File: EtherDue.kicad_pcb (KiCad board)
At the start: 4 copper layers, 185 x 104 mm, 619 parts, among them IC201 ATSAM3X8E, IC301 ATMEGA16U2, IC601 W5100, P101 CONN_02X04, P102 MSTBV3, P103 MSTBV3, P104 MSTBV6, P1101 CONN_01X02, P1102 CONN_01X02, P1201 CONN_01X02, P1202 CONN_01X02, P1301 CONN_01X02, P1302 CONN_01X02, P1401 CONN_01X02, P1402 CONN_01X02, P301 USB_5PIN_SHELL, P401 USB_5PIN_SHELL, P801 MSTBV2, P901 677006144621, P902 677006144621, Q1001 BSS308, Q101 IPB020NE7N3G, Q102 IPB020NE7N3G, Q1501 BSS123, Q1502 BSS123, Q1601 BSS123, Q1602 BSS123, Q1701 BSS123, Q1702 BSS123, Q1703 BSS308, Q1704 BSS308, Q1801 BSS123, Q1802 BSS123, Q1803 BSS308, Q1804 BSS308, Q1901 BSS123, Q1902 BSS123, Q1903 BSS308, Q1904 BSS308, Q501 BC847BSMD, Q601 2N7002, SW1701 SW_PUSH, SW1801 SW_PUSH, SW1901 SW_PUSH, SW201 ERASE, SW202 RESET, U1001 AD7294BSUZ, U101 AD7415, U1101 ADL5513, U1102 REG101NA-5, U1201 ADL5513, U1202 REG101NA-5, U1301 ADL5513, U1302 REG101NA-5, U1401 ADL5513, U1402 REG101NA-5, U1501 4013_with_supply, U1701 MCP6H04, U1702 INA207, U1703 MEU1S1212ZC, U1801 INA207, U1802 MEU1S1212ZC, U1901 INA207, U1902 MEU1S1212ZC, U202 FDN340P, U203 LMV358IPWR, U501 POWERJACK, U502 LM2734Y, U503 FDN340P, U504 FDN340P, U505 NCP1117ST33T3G, U602 HY931147C, U603 APX811-31UG-7, U701 MICROSD, U702 24AA025E48, U801 TPS7A4501DCQT, U802 TPS7A4501DCQT, U803 TPS7A4501DCQT, U804 REG101NA-5, U901 TJA1040T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

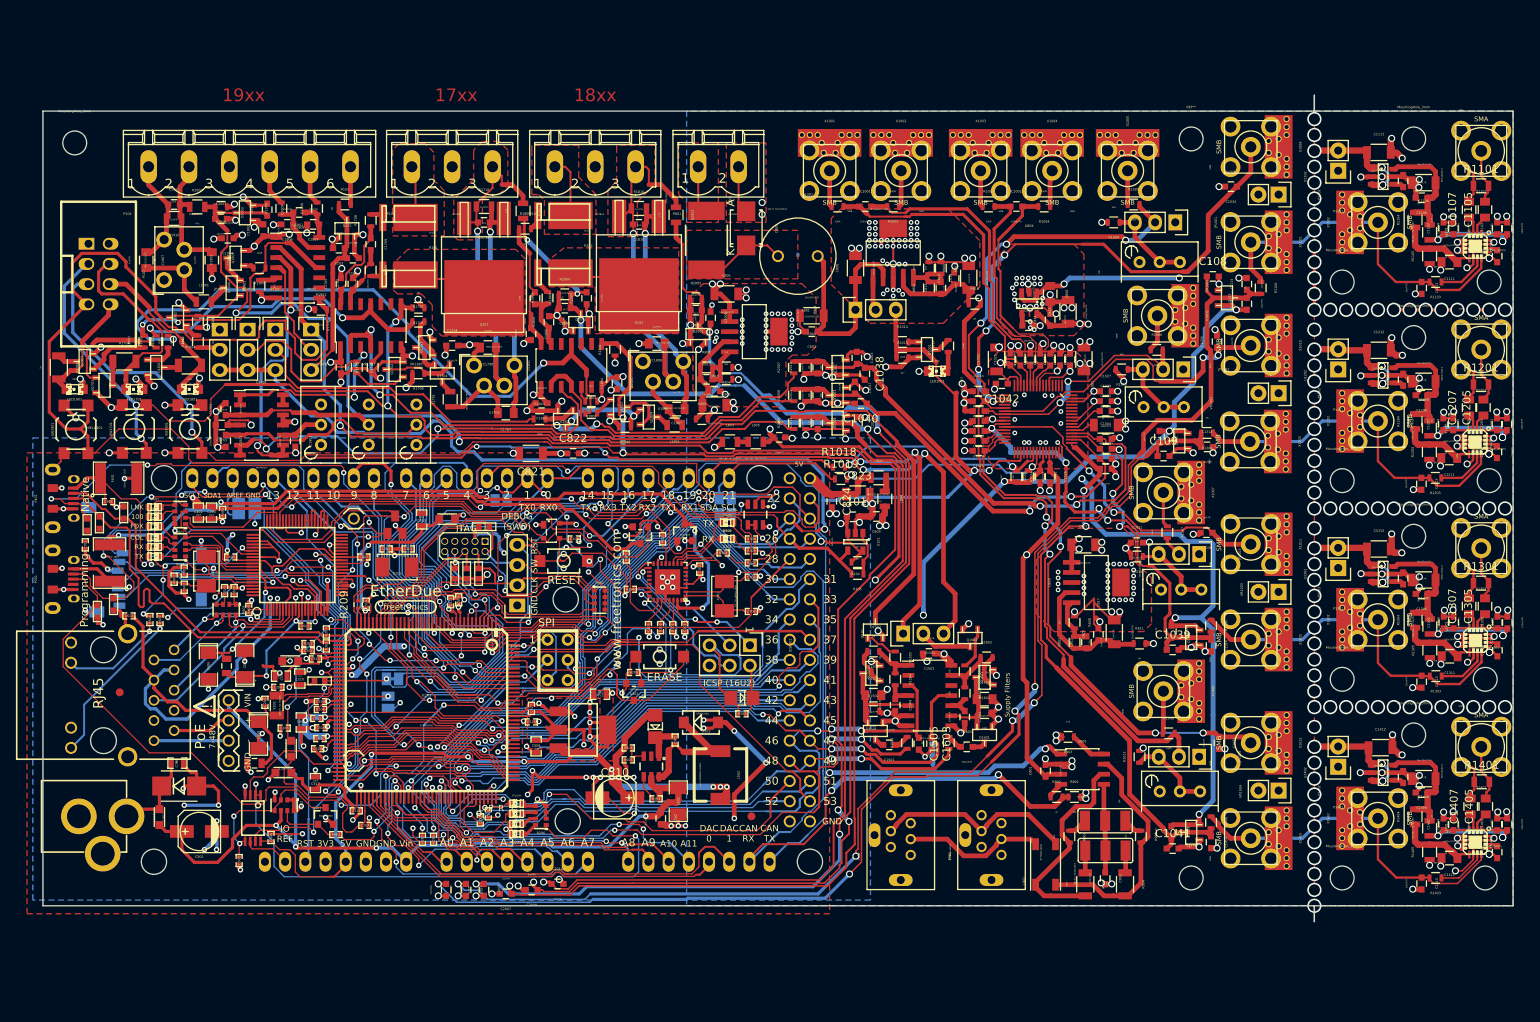
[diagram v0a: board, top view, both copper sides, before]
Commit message: fixed missing Rs before Potis - fixed (removed) AD7294 Vpp connection
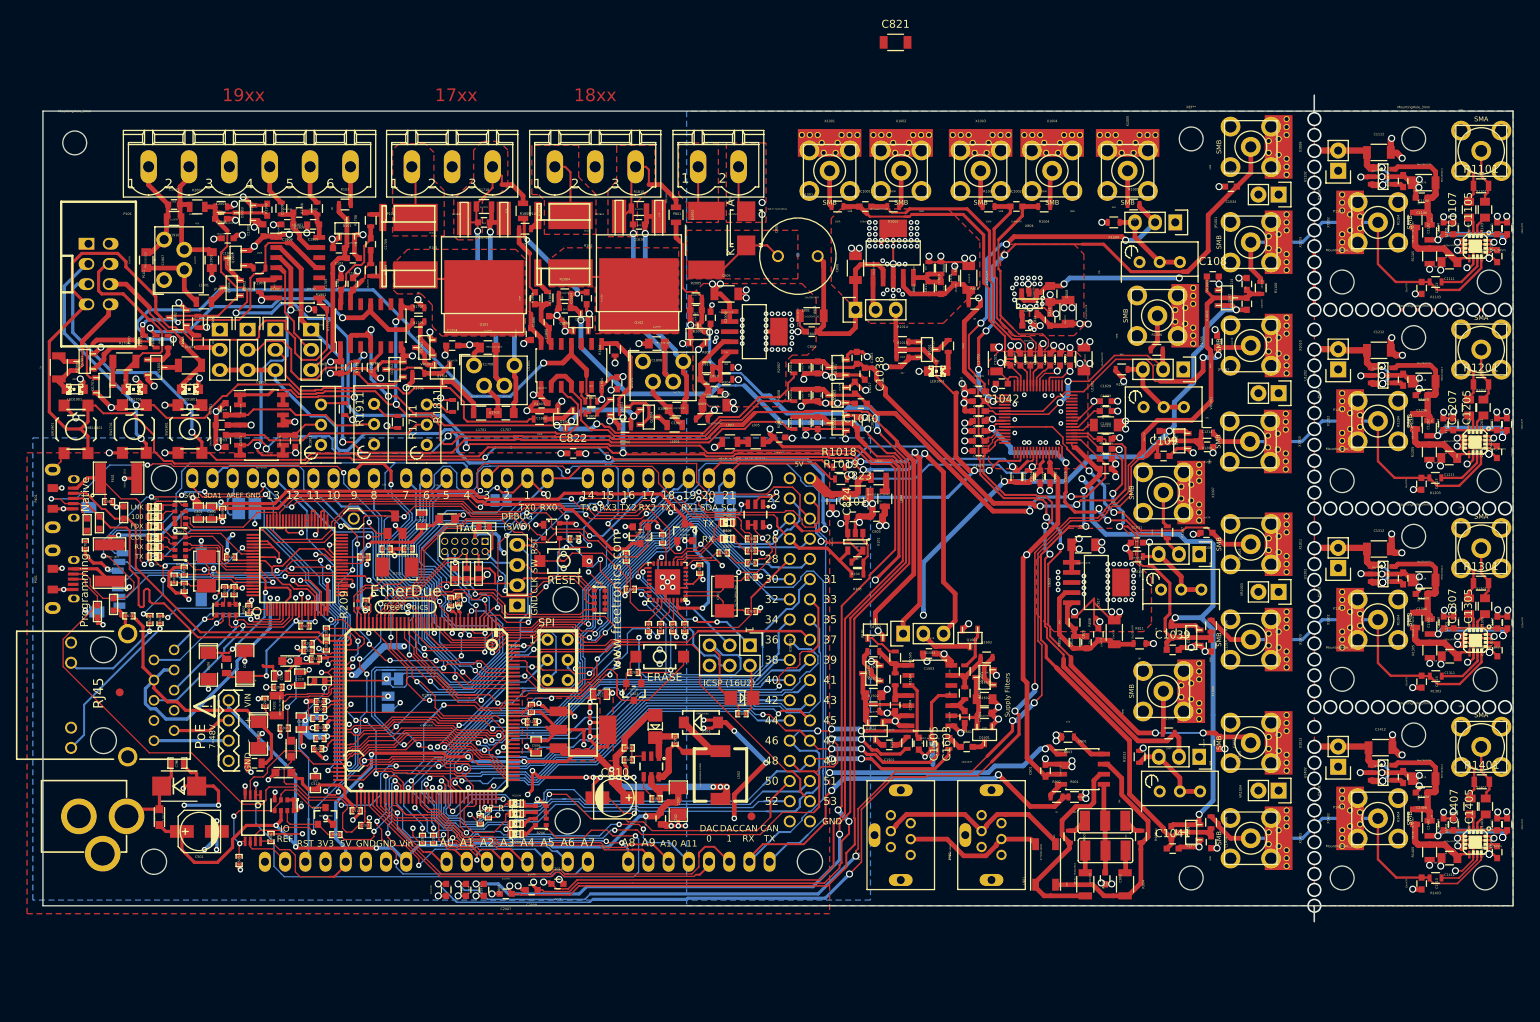
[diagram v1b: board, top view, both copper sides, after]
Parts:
- removed C1027: 100n/X7R, Capacitors_SMD:C_0603
- added R1711: 91k, Resistors_SMD:R_0603, F.Cu at (101.7, 80.7)
- added R1811: 91k, Resistors_SMD:R_0603, F.Cu at (108.6, 78.7)
- added R1911: 91k, Resistors_SMD:R_0603, F.Cu at (95.0, 79.1)
- L802, L803: value WE-CBF-742792093 -> WE-CBF-742792040
- R2012: value TBD -> 6k8
- VR1701, VR1801, VR1901: value 100k -> 10k
- moved C821 69.1 mm to (164.3, 33.0), turned to 0 degrees
- moved L1701 4.27 mm to (112.2, 79.6), turned to 180 degrees
- moved VR1801 1.30 mm to (105.3, 83.6)
- moved VR1701 0.68 mm to (98.7, 83.5)
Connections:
- U1001 pad 62: /Analog I/O/+5VA -> Net-(U1001-Pad62)
- U1001 pad 63: /Analog I/O/+5VA -> Net-(U1001-Pad63)
- VR1701 pad 3: /eFuse 1 (10A)/+12V -> Net-(R1711-Pad1)
- VR1801 pad 3: /eFuse 1 (10A)/+12V -> Net-(R1811-Pad1)
- VR1901 pad 3: /eFuse 1 (10A)/+12V -> Net-(R1911-Pad1)
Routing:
- net /Fuse-Reset A/Reset\: track 177.2 -> 203.8 mm
- net /eFuse 1 (10A)/+12V: track 258.4 -> 242.2 mm, vias 20 -> 23
- net GND: track 2410.2 -> 2396.7 mm, vias 567 -> 565
- net /Analog I/O/+5VA: track 161.1 -> 154.6 mm, vias 15 -> 14
- net Net-(L1701-Pad2): track 1.66 -> 6.32 mm
- net Net-(C1707-Pad2): track 9.55 -> 5.33 mm
- net +3.3V: track 152.3 -> 148.5 mm
- net Net-(R1711-Pad1): track 0.00 -> 3.73 mm
- net Net-(R1811-Pad1): track 0.00 -> 3.64 mm
- net Net-(R1911-Pad1): track 0.00 -> 3.05 mm
- net PIN24: track 268.4 -> 271.0 mm
- net /eFuse 3 (60A)/ISense: track 85.9 -> 88.0 mm
- net Net-(JP1801-Pad2): track 37.6 -> 39.7 mm
- net Net-(U1701-Pad6): track 56.6 -> 54.5 mm
- net Net-(C1701-Pad1): track 19.0 -> 19.9 mm
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
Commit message: Rev B. Layout - Gerber/BOM need to be reexported
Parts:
- added C612: 100nF, Capacitors_SMD:C_0402, F.Cu at (147.0, 99.2)
- added C613: 100nF, Capacitors_SMD:C_0402, F.Cu at (147.8, 94.8)
- added U601: 24LC64T-I/OT, w_smd_trans:sot23-5, F.Cu at (147.4, 97.0)
- C1001, C1002: value 100n/X7R -> 1n/X7R
- C1005, C1007, C1011, C1014: value 100n/X7R -> 100p/X7R
- C501, C510: footprint Capacitors_SMD:c_elec_5x5.3 -> Capacitors_SMD:c_elec_6.3x5.8
- C604, C606, C608: value 10uF 6.3V A TANT -> 10u/25V/X7R
- F801: value SMD100F -> SMD050F; footprint eagle-switch-raychem:SMD050F -> zeilhofer:SMD050F
- L601, L602: value 1uH 250mA -> WE-CBF-742792093
- R101, R102: value Shunt -> Shunt 10mOhm
- R1704, R1804, R1904, R904, R905: footprint Resistors_SMD:R_1206 -> Resistors_SMD:R_0805
- R2010, R2011: value 6k8 -> DNP
- R906, R907: footprint Resistors_SMD:R_0603 -> Resistors_SMD:R_0805
- U1702, U1801, U1901: value INA207 -> INA206
- moved C821 69.1 mm to (118.6, 84.7), turned to 180 degrees
- moved U1902 6.20 mm to (76.1, 58.0), turned to 270 degrees
- moved U1703 6.06 mm to (116.2, 77.2), turned to 180 degrees
- moved U1802 6.04 mm to (137.3, 76.7), turned to 180 degrees
- moved R308 2.86 mm to (143.5, 94.4)
- moved R309 2.67 mm to (143.6, 96.4)
- moved R305 2.30 mm to (144.0, 97.8), turned to 270 degrees
- moved L501 1.81 mm to (70.8, 132.0)
- moved C303 1.45 mm to (145.4, 101.5)
- moved C304 1.11 mm to (145.4, 103.8)
- moved C501 0.76 mm to (76.6, 133.0)
- moved R1811 0.71 mm to (108.1, 79.2)
- moved C510 0.58 mm to (128.6, 128.4)
- moved R304 0.21 mm to (142.6, 97.4)
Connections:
- U702 pad 5: GND -> +5V
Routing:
- net GND: track 2396.7 -> 2377.9 mm, vias 565 -> 568
- net Net-(R1803-Pad2): track 86.8 -> 94.1 mm
- net Net-(SJ701-Pad2): track 8.48 -> 13.7 mm, vias 1 -> 2
- net Net-(SJ702-Pad2): track 3.15 -> 8.23 mm, vias 1 -> 2
- net /PA-Monitor Power Supply/VIN: track 136.0 -> 130.9 mm
- net +5V: track 148.9 -> 153.1 mm, vias 15 -> 16
- net /eFuse 3 (60A)/Gate: track 13.3 -> 17.4 mm
- net /eFuse 3 (60A)/Source: track 16.1 -> 19.9 mm
- net /Connectors/RX: track 75.0 -> 71.2 mm
- net PIN50: track 58.2 -> 61.6 mm
- net /eFuse 1 (10A)/Source: track 44.0 -> 40.9 mm
- net /eFuse 2 (10A)/Source: track 45.5 -> 42.4 mm
- net Net-(L901-Pad1): track 30.0 -> 32.8 mm
- net PIN28: track 55.6 -> 58.3 mm
- net VIN_JACK: track 221.6 -> 223.9 mm
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- added copper zone on F.Cu, net Net-(F801-Pad1)
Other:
- board text added: "Rev. B"

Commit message: RevC
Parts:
- added R1712: 4k7, FT:0603, F.Cu at (104.3, 67.9)
- added R1812, R1912: 4k7, FT:0603, F.Cu at (149.5, 153.7)
- moved R1707 1.14 mm to (104.3, 69.2)
- moved Q1703 0.45 mm to (105.3, 71.7), turned to 180 degrees
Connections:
- net /eFuse 1 (10A)/+12V renamed /+12V_Fuse
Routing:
- net Net-(Q1703-PadG): track 5.06 -> 1.95 mm
- net Net-(Q1703-PadD): track 3.81 -> 1.38 mm
- net /+12V_Fuse: track 242.5 -> 244.2 mm
- net Net-(R1703-Pad2): track 40.7 -> 41.6 mm
- added copper zone on Inner.VCC, net /eFuse 1 (10A)/+12V
- removed copper zone on Inner.VCC, net /+12V_Fuse
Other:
- board text added: "HF-AMP 400 (c) Otelo eGen 2019 CC-BY-SA-3.0 derived from EtherDue (which is derived from Arduino Due)"
- board text added: "Rev. C"
- board text removed: "HF-AMP 400 (c) Otelo eGen 2015 CC-BY-SA-3.0 derived from EtherDue (which is derived from Arduino Due)"
- board text removed: "Rev. B"
